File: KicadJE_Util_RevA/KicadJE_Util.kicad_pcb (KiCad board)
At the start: 2 copper layers, 159 x 128 mm, 224 parts, among them J101 Out1, J102 Out2, J103 In1.1, J104 In1.2, J105 In1.3, J106 SS_In2, J201 Out2.1, J202 Out2.2, J203 In2.1, J204 CV2.1, J205 In2.2, J206 CV2.2, J301 In3.1, J302 Out3.1, J303 Out3.2, P101 HEADER_2x5_Doepfer, P201 HEADER_2x5_Doepfer, P301 HEADER_2x5_Doepfer, U101 TL072, U102 TL072, U201 TL072, U202 TL072, U301 TL072, U302 TL072, U303 TL072, U304 TL072

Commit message: Placing IO components
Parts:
- C201, C202, C203, C204, C205, C206, C207, C208, C209, C210, C211, C212, D201, D202, D204, D205, D206, D207, D208, D209, P101, P201, P301, R201, R202, R203, R204, R205, R206, R207, R208, R209, R210, R211, R212, R213, R214, R215, R216, R217, R218, R219, R220, R221, R222, R223, R224, R225, R226, R227, R228, R229, TP209, TP210, U201, U202: moved to B.Cu
- moved J201 207.6 mm to (59.5, 145.0), turned to 270 degrees
- moved J202 203.4 mm to (79.5, 145.0), turned to 90 degrees
- moved J204 167.5 mm to (59.8, 125.3), turned to 270 degrees
- moved J205 158.7 mm to (80.0, 115.0), turned to 90 degrees
- moved J203 156.6 mm to (59.8, 115.1), turned to 270 degrees
- moved J206 152.5 mm to (79.5, 125.0), turned to 90 degrees
- moved J302 135.2 mm to (101.0, 135.0), turned to 90 degrees
- moved J303 132.0 mm to (101.0, 145.0), turned to 90 degrees
- moved RV201 122.3 mm to (72.5, 67.5)
- moved P201 117.0 mm to (75.0, 56.0), turned to 90 degrees
- moved P101 116.4 mm to (118.5, 53.5), turned to 270 degrees
- moved H202 116.1 mm to (19.5, -67.0)
- moved H204 116.1 mm to (19.5, -62.0)
- moved C101 115.6 mm to (161.6, 98.7)
- moved C102 115.6 mm to (167.5, 98.7)
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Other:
- board size 159 x 128 mm -> 143 x 128 mm

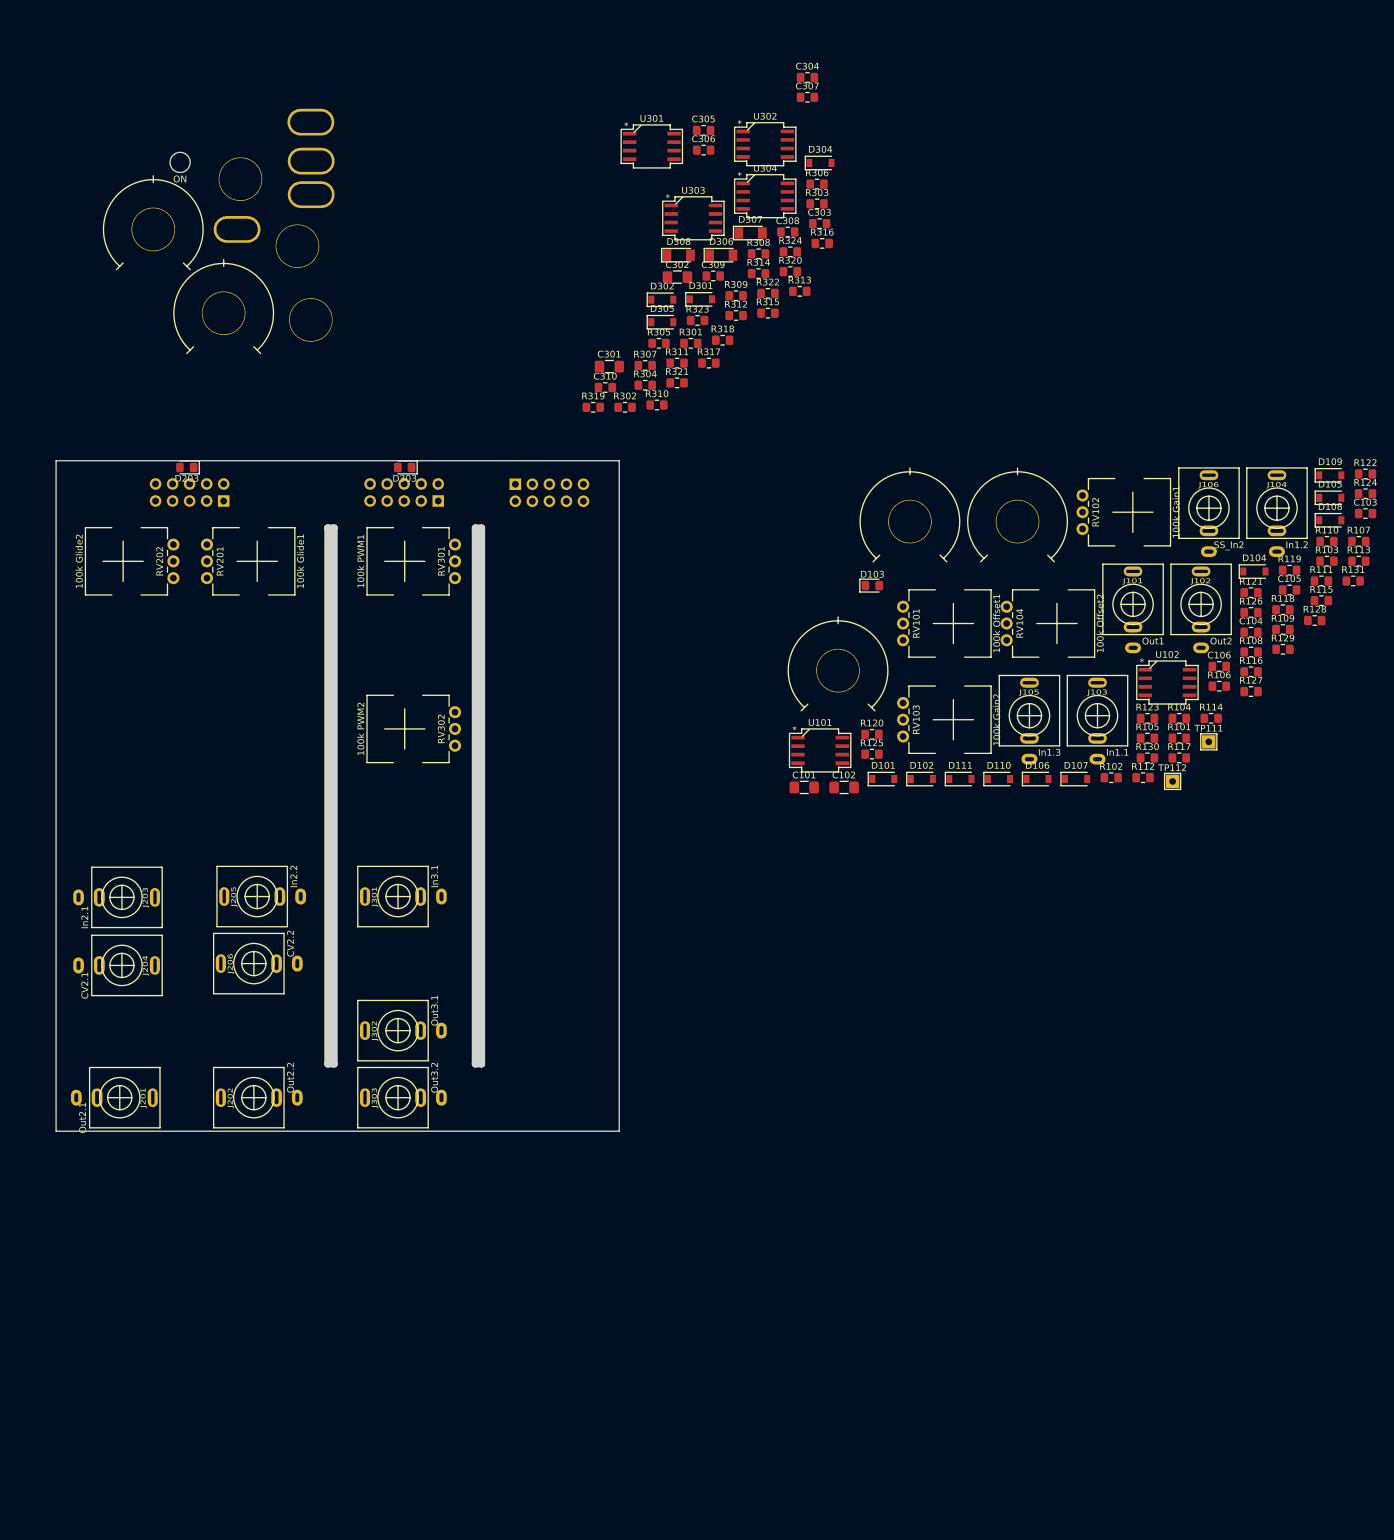
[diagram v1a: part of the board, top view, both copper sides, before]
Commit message: Faceplace komp placed
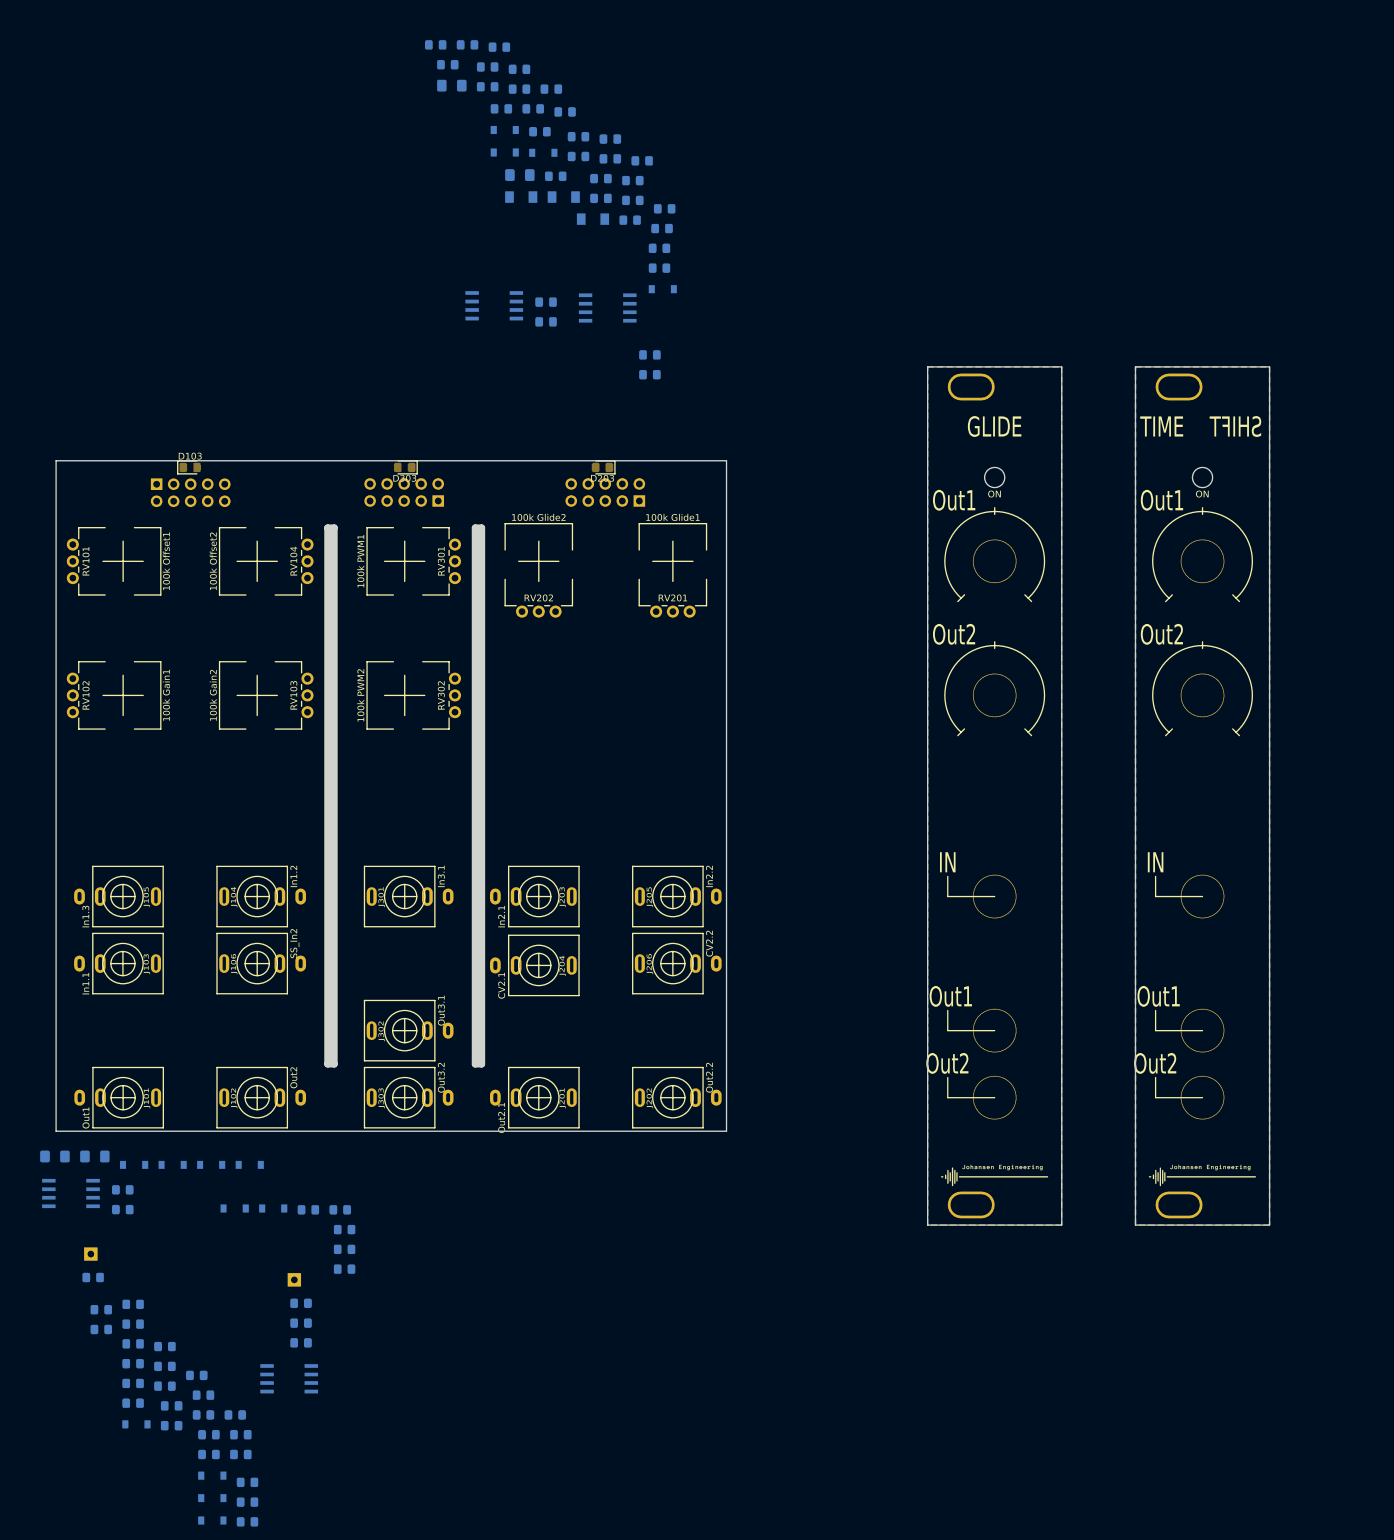
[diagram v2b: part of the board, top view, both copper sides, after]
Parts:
- removed H302, H303, H304, H305: MountingHole_Pad, AJ:MountingHole_Eurorack3
- removed the TP108 at (166.6, 81.3)
- removed TP109: Gain2, AJ:Pot_6m3_scale1
- removed TP110: Gain1, AJ:Pot_6m3_scale1
- removed U303, U304: TL072, AJ-Dropbox-Kicad:AJ_SO-8_5.3x6.2mm_P1.27mm
- added G***: LOGO, AJ:Johansen_engineering_logo_20mm, F.Cu at (190.0, 156.8)
- added G***: LOGO, AJ:Johansen_engineering_logo_20mm, F.Cu at (221.0, 156.8)
- added H102: MountingHole_Pad, AJ:MountingHole_Eurorack3, F.Cu at (186.5, 39.0)
- added H102: MountingHole_Pad, AJ:MountingHole_Eurorack3, F.Cu at (217.5, 39.0)
- added H103: MountingHole_Pad, AJ:MountingHole_Eurorack3, B.Cu at (186.5, 161.0)
- added H103: MountingHole_Pad, AJ:MountingHole_Eurorack3, B.Cu at (217.5, 161.0)
- added H301: ON, AJ:LED_Hole_3mm, F.Cu at (190.0, 52.5)
- added TP301: In1, AJ:Jack_6m3, F.Cu at (190.0, 115.0)
- added TP302: Tri, AJ:Jack_6m3, F.Cu at (190.0, 135.0)
- added TP303: SQ, AJ:Jack_6m3, F.Cu at (190.0, 145.0)
- added TP304: PWM1, AJ:Pot_6m3_scale1, F.Cu at (190.0, 65.0)
- added TP305: PWM2, AJ:Pot_6m3_scale1, F.Cu at (190.0, 85.0)
- C101, C102, C103, C104, C105, C106, C301, C302, C303, C304, C305, C306, C307, C308, C309, C310, D101, D102, D104, D105, D106, D107, D108, D109, D110, D111, D301, D302, D304, D305, D306, D307, D308, R101, R102, R103, R104, R105, R106, R107, R108, R109, R110, R111, R112, R113, R114, R115, R116, R117, R118, R119, R120, R121, R122, R123, R124, R125, R126, R127, R128, R129, R130, R131, R301, R302, R303, R304, R305, R306, R307, R308, R309, R310, R311, R312, R313, R314, R315, R316, R317, R318, R319, R320, R321, R322, R323, R324, TP111, TP112, U101, U102, U301, U302: moved to B.Cu
- moved R122 228.6 mm to (78.6, 208.3)
- moved D109 228.3 mm to (73.3, 208.1)
- moved R124 224.6 mm to (78.6, 205.3)
- moved D105 223.8 mm to (73.3, 204.7)
- moved C103 220.6 mm to (78.6, 202.4)
- moved D108 219.3 mm to (73.3, 201.4)
- moved R107 215.3 mm to (77.6, 198.2)
- moved R110 215.3 mm to (72.8, 198.2)
- moved R103 211.6 mm to (72.8, 195.3)
- moved R113 211.6 mm to (77.6, 195.3)
- moved R119 210.0 mm to (67.2, 193.9)
- moved D104 209.7 mm to (62.0, 193.7)
- moved R111 208.0 mm to (72.0, 192.3)
- moved R131 208.0 mm to (76.7, 192.3)
- moved C105 206.4 mm to (67.2, 191.0)
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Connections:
- U301 pad 1: (no net) -> Out3.1
- U301 pad 2: (no net) -> Net-(RV301-Pad2)
- U301 pad 3: (no net) -> Net-(R315-Pad2)
- U301 pad 5: Net-(R315-Pad2) -> Net-(C308-Pad2)
- U301 pad 6: Net-(RV301-Pad2) -> Net-(R312-Pad2)
- U301 pad 7: Out3.1 -> Out3.2
- U302 pad 1: (no net) -> PosPk1
- U302 pad 2: (no net) -> PosPk1
- U302 pad 3: (no net) -> Net-(C309-Pad2)
- U302 pad 5: Net-(C308-Pad2) -> Net-(C310-Pad2)
- U302 pad 6: Net-(R312-Pad2) -> NegPk1
- U302 pad 7: Out3.2 -> NegPk1
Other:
- board size 143 x 128 mm -> 240 x 128 mm
- board text added: "GLIDE"
- board text added: "IN"
- board text added: "Out1"
- board text added: "Out2"
- board text added: "SHIFT"
- board text added: "TIME"

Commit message: Update KicadJE_Util.kicad_pcb
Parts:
- removed H201: ON, AJ:LED_Hole_3mm
- removed H202, H203, H204, H205: MountingHole_Pad, AJ:MountingHole_Eurorack3
- removed the TP101 at (1.00, 84.5)
- removed the TP106 at (21.0, 135.0)
- removed TP201: Tri, AJ:Jack_6m3
- removed TP202: SQ, AJ:Jack_6m3
- removed TP203: In1, AJ:Jack_6m3
- removed TP204: In2, AJ:Jack_6m3
- removed TP205: In3, AJ:Jack_6m3
- removed TP206: SS, AJ:Jack_6m3
- removed TP207: Glide1, AJ:Pot_6m3_scale1
- removed TP208: Glide2, AJ:Pot_6m3_scale1
- added G***: LOGO, AJ:Johansen_engineering_logo_20mm, F.Cu at (249.5, 156.0)
- added H101: ON, AJ:LED_Hole_3mm, F.Cu at (213.0, 51.0)
- added H102: MountingHole_Pad, AJ:MountingHole_Eurorack3, F.Cu at (199.5, 39.0)
- added H103: MountingHole_Pad, AJ:MountingHole_Eurorack3, B.Cu at (199.5, 161.0)
- added H104: MountingHole_Pad, AJ:MountingHole_Eurorack3, F.Cu at (226.5, 39.0)
- added H105: MountingHole_Pad, AJ:MountingHole_Eurorack3, B.Cu at (226.5, 161.0)
- added TP101: Tri, AJ:Jack_6m3, F.Cu at (203.0, 84.5)
- added TP101: Oct, AJ:Pot_6m3, F.Cu at (223.0, 84.5)
- added TP102: SQ, AJ:Jack_6m3, F.Cu at (203.0, 115.0)
- added TP103: In1, AJ:Jack_6m3, F.Cu at (223.0, 125.0)
- added TP105: In3, AJ:Jack_6m3, F.Cu at (223.0, 145.0)
- added TP106: HS, AJ:Jack_6m3, F.Cu at (203.1, 145.0)
- added TP106: SS, AJ:Jack_6m3, F.Cu at (223.0, 135.0)
- added TP107: OFF1, AJ:Pot_6m3_scale1, F.Cu at (223.0, 65.0)
- added TP107: FM, AJ:Jack_6m3, F.Cu at (223.0, 115.0)
- added TP108: PWM, AJ:Jack_6m3, F.Cu at (203.0, 125.0)
- added TP112: Fine, AJ:Pot_6m3_scale1, F.Cu at (1.00, 84.5)
- added TP112: Fine, AJ:Pot_6m3_scale1, F.Cu at (203.0, 65.0)
- C201, C202, D201, D202, R201: moved to F.Cu
- moved D205 301.0 mm to (120.0, 225.0)
- moved R216 298.0 mm to (117.5, 229.5)
- moved R229 294.2 mm to (132.5, 220.0)
- moved R217 291.7 mm to (132.5, 229.5)
- moved TP210 291.1 mm to (143.5, 220.0)
- moved R228 277.1 mm to (117.5, 220.0)
- moved TP209 269.6 mm to (114.0, 220.0)
- moved D207 267.8 mm to (135.0, 225.0)
- moved C211 249.0 mm to (132.7, 170.6)
- moved R220 249.0 mm to (137.5, 170.6)
- moved C203 248.4 mm to (154.6, 200.1)
- moved C205 248.4 mm to (140.4, 187.7)
- moved C207 248.4 mm to (149.2, 199.4)
- moved C209 248.4 mm to (154.6, 203.1)
- moved C212 248.4 mm to (149.2, 193.5)
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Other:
- board size 240 x 128 mm -> 268.5 x 128 mm
- board text added: "CV"
- board text added: "Gain1"
- board text added: "Gain2"
- board text added: "In1"
- board text added: "In2"
- board text added: "Inv1"
- board text added: "Inv2"
- board text added: "Offset1"
- board text added: "Offset2"

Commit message: Update KicadJE_Util.kicad_pcb
Time shift placed
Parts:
- removed TP101: Tri, AJ:Jack_6m3
- removed TP101 (x2): Oct, AJ:Pot_6m3
- removed TP104: In2, AJ:Jack_6m3
- removed the TP106 at (223.0, 135.0)
- removed the TP111 at (203.0, 95.0)
- removed TP115: 3m5 jack, AJ:Jack_6m3
- added TP107: Gain, AJ:Pot_6m3_scale1, F.Cu at (21.0, 84.5)
- C301, C302, D301, D302, R101, R301: moved to F.Cu
- moved R304 131.5 mm to (105.0, 141.5), turned to 180 degrees
- moved R101 127.6 mm to (74.0, 51.0)
- moved R305 114.0 mm to (100.0, 131.5), turned to 180 degrees
- moved D304 107.7 mm to (99.0, 118.5)
- moved R302 105.4 mm to (100.5, 111.5), turned to 180 degrees
- moved R307 99.9 mm to (105.0, 111.5), turned to 180 degrees
- moved D305 99.4 mm to (104.3, 118.5)
- moved R306 97.3 mm to (100.0, 141.5), turned to 180 degrees
- moved R303 90.5 mm to (105.0, 131.5), turned to 180 degrees
- moved R311 90.3 mm to (98.5, 105.2), turned to 270 degrees
- moved C305 88.0 mm to (105.8, 105.2), turned to 270 degrees
- moved R310 86.4 mm to (96.2, 94.8), turned to 270 degrees
- moved U301 84.2 mm to (102.0, 100.0)
- moved C306 80.6 mm to (100.2, 94.8), turned to 270 degrees
- moved R317 75.7 mm to (106.5, 89.0), turned to 180 degrees
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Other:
- board text added: "CV1"
- board text added: "CV2"
- board text added: "Glide1"
- board text added: "Glide2"
- board text added: "Phase1"
- board text added: "Phase2"
- board text removed: "FM"
- board text removed: "Fine"
- board text removed: "HS"
- board text removed: "In 1"
- board text removed: "In 2"
- board text removed: "In 3"
- board text removed: "OCT"
- board text removed: "PWM"
- board text removed: "SQ"
- board text removed: "SS"
- board text removed: "Saw"
- board text removed: "Sine"
- board text removed: "Tri"
- board text removed: "in"
- board text removed: "out"

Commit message: Timeshift routed
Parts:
- moved D306 22.5 mm to (110.2, 109.0)
- moved D301 17.3 mm to (93.2, 54.8)
- moved D302 17.3 mm to (110.8, 54.8)
- moved C307 16.5 mm to (107.8, 108.2)
- moved R310 16.5 mm to (105.8, 108.2)
- moved C305 13.5 mm to (98.2, 94.0), turned to 90 degrees
- moved C308 13.2 mm to (96.2, 100.8), turned to 90 degrees
- moved R315 12.9 mm to (107.8, 104.5), turned to 90 degrees
- moved R316 11.5 mm to (96.2, 97.0)
- moved C306 11.2 mm to (105.8, 104.5), turned to 90 degrees
- moved C301 8.75 mm to (98.2, 58.5), turned to 0 degrees
- moved C302 8.26 mm to (106.8, 58.5), turned to 0 degrees
- moved R312 5.77 mm to (96.2, 104.5), turned to 90 degrees
- moved R311 0.77 mm to (98.2, 104.5), turned to 90 degrees
- moved D307 0.75 mm to (96.2, 87.5)
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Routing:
- net +12VA: track 0.00 -> 95.2 mm, vias 0 -> 2
- net -12VA: track 0.00 -> 80.6 mm
- net Out3.1: track 0.00 -> 60.6 mm
- net Out3.2: track 0.00 -> 55.8 mm, vias 0 -> 2
- net In3.1a: track 0.00 -> 40.1 mm, vias 0 -> 2
- net GND: track 0.00 -> 39.1 mm, vias 0 -> 28
- net Net-(RV301-Pad2): track 0.00 -> 39.0 mm
- net NegPk1: track 0.00 -> 24.6 mm, vias 0 -> 2
- net Net-(R316-Pad2): track 0.00 -> 22.4 mm, vias 0 -> 2
- net Net-(D307-Pad1): track 0.00 -> 18.2 mm, vias 0 -> 2
- net PosPk1: track 0.00 -> 15.8 mm
- net Net-(D304-Pad2): track 0.00 -> 12.2 mm
- net Net-(C308-Pad2): track 0.00 -> 11.5 mm
- net Net-(J303-PadT): track 0.00 -> 10.7 mm
- net Net-(J302-PadT): track 0.00 -> 10.3 mm
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
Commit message: Update KicadJE_Util.kicad_pcb
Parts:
- added G***: LOGO, AJ:Johansen_engineering_logo_20mm, F.Cu at (102.0, 125.0)
- C101, C102, D101, D102: moved to F.Cu
- moved U202 112.6 mm to (142.0, 90.0), turned to 180 degrees
- moved D102 102.8 mm to (79.0, 54.8), turned to 270 degrees
- moved D101 100.8 mm to (61.2, 54.8), turned to 90 degrees
- moved C102 99.5 mm to (73.5, 58.5)
- moved C101 99.1 mm to (66.1, 58.5)
- moved U102 93.0 mm to (70.0, 94.0), turned to 180 degrees
- moved D108 89.7 mm to (57.8, 111.8), turned to 180 degrees
- moved U201 88.1 mm to (122.0, 90.0), turned to 180 degrees
- moved D109 86.4 mm to (57.8, 121.8), turned to 180 degrees
- moved D105 83.0 mm to (62.8, 121.8), turned to 180 degrees
- moved D104 82.8 mm to (62.8, 111.8), turned to 180 degrees
- moved R107 79.8 mm to (62.2, 118.5)
- moved R113 77.2 mm to (58.1, 118.5)
- moved R115 73.9 mm to (82.0, 118.5), turned to 180 degrees
- moved R106 73.7 mm to (64.0, 105.2), turned to 90 degrees
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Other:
- board text added: "TimeShift"
- board text added: "TimeShift Rev A 22/03-2020 Johansen Engineering"
- board text removed: "AS3340 Rev A - 07/03-2020 Johansen Engineering"
